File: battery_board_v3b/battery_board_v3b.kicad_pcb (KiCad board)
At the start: 4 copper layers, 88 x 94.5 mm, 204 parts, among them IC2 PCT2075DP,118, IC3 RP2040_QFN56, IC4 LT3652IMSE#PBF, J1 Bypass, J10 Jetson, J11 BM04B-SRSS-TB(LF)(SN), J14 Solar, J15 FC, J16 I2C Multiplexer Breakout, J17 ISS Foot, J18 Screw_Terminal_01x02, J19 BM04B-SRSS-TB(LF)(SN), J2 Heater, J20 CAN1, J21 BM04B-SRSS-TB(LF)(SN), J22 CAN2, J23 Conn_ARM_JTAG_SWD_10, J24 USB_B_Micro, J25 Life Makes Lemonade, J26 BM04B-SRSS-TB(LF)(SN), J27 I2C0 Breakout, J3 BURN, J4 CHARGE, J5 Foot0, J6 Foot1, J7 Foot2, J8 Foot3, J9 RBF, K1 APAN3105, Q1 IRF7458, Q10 IRLML2803, Q11 NDS8434, Q2 IRF7458, Q3 MBT2222ADW1T1, Q4 MMBT2222AT, Q5 MBT2222ADW1T1, Q6 IRLML2803, Q7 IRLML2803, Q8 NDS8434, Q9 NDS8434, SW1 KMR2, SW2 KMR2, U1 R5460N208AA, U10 TLVH431 DBZ SOT-23, U11 MCP25625-E/ML, U12 INA219AxD, U13 MAX706RESA, U14 INA219AxD, U2 1049, U3 TPS54226PWPRPWP14_2P31X2P46-L, U4 1049, U5 TPS54226PWPRPWP14_2P31X2P46-L, U6 TPS7A4501DCQT, U7 ADS1015IDGS, U8 W25Q128JV, U9 AD8495, Y1 Crystal_GND24, Y2 Crystal_GND24

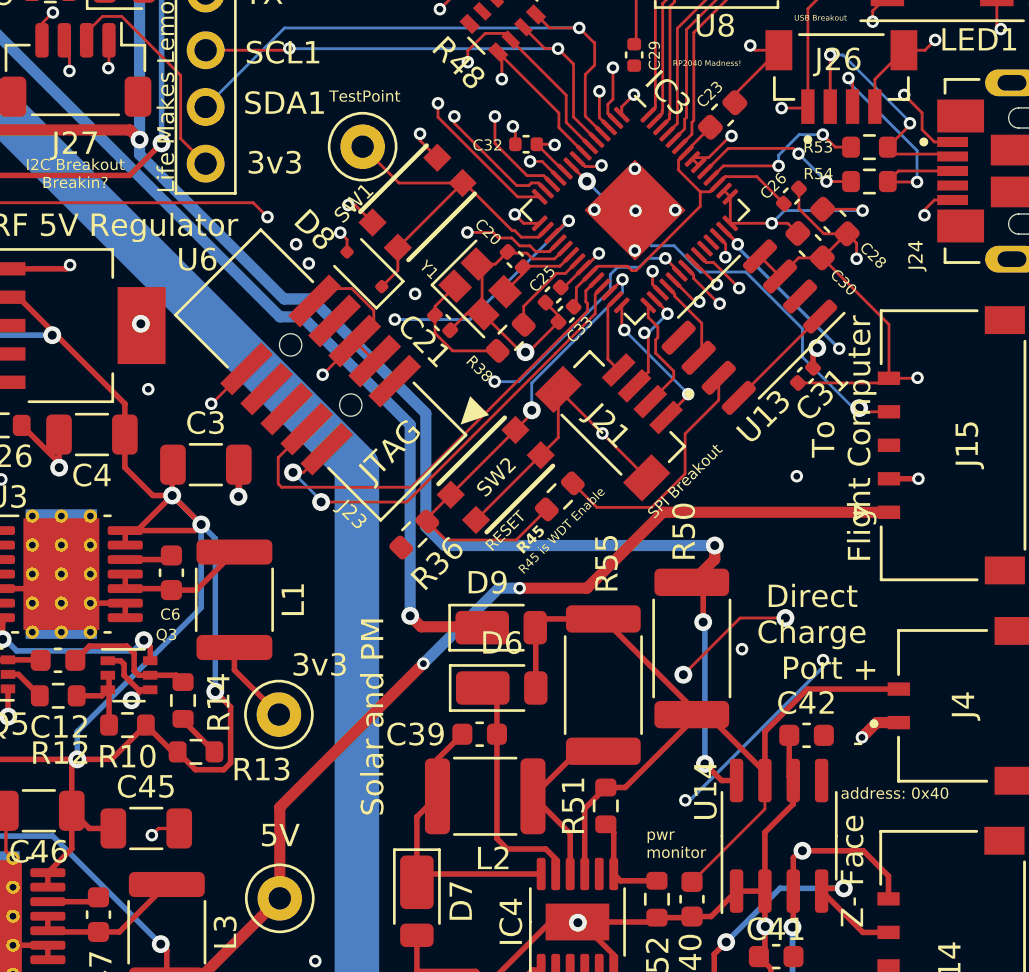
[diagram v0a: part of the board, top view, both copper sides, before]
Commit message: Adjusted Postitioning of Resistors
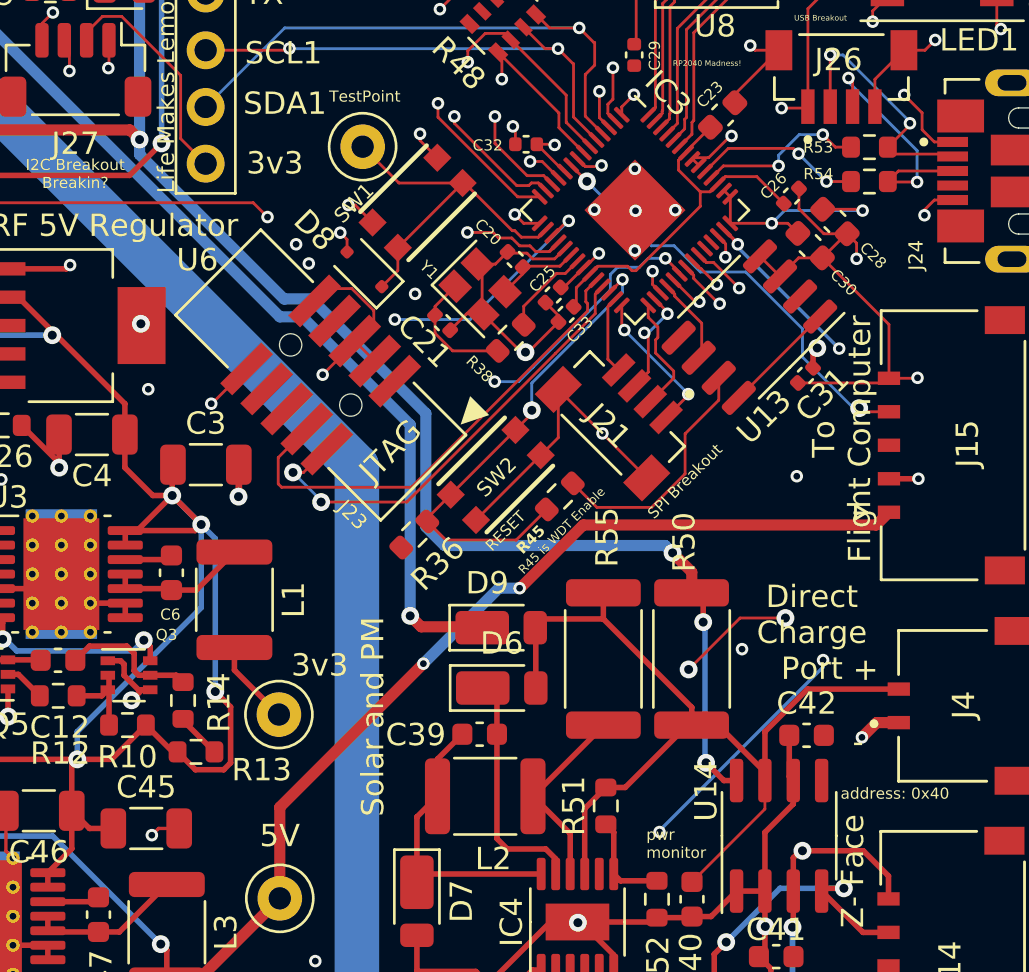
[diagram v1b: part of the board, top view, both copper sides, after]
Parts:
- moved R55 1.17 mm to (176.2, 98.1)
- moved R50 0.47 mm to (180.2, 98.1)
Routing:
- net PACK+: track 215.3 -> 213.1 mm
- net 5V_enable: track 73.6 -> 74.8 mm
- net VBATT_SENSE: track 41.0 -> 42.2 mm
- net Net-(IC4-SENSE): track 8.16 -> 8.66 mm

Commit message: Update battery_board_v3b.kicad_pcb
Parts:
- moved TP9 12.4 mm to (151.2, 115.3)
- moved R1 4.05 mm to (128.0, 110.2)
- moved C46 2.80 mm to (153.7, 105.5)
- moved R61 2.76 mm to (146.2, 113.8)
- moved C47 2.74 mm to (156.4, 109.7)
- moved C43 2.74 mm to (145.3, 105.1)
- moved C45 2.74 mm to (158.5, 105.8)
- moved C48 2.74 mm to (144.2, 111.3)
- moved C49 2.74 mm to (144.2, 109.7)
- moved L3 2.74 mm to (159.4, 110.5)
- moved U5 2.74 mm to (151.2, 109.8)
- moved C44 2.74 mm to (144.2, 106.6)
- moved R18 2.74 mm to (144.2, 108.2)
- moved R16 2.74 mm to (146.5, 107.4)
- moved R20 2.74 mm to (146.5, 110.4)
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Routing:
- net Net-(C5-Pad1): track 8.32 -> 11.3 mm
- net 5V_enable: track 74.8 -> 72.1 mm
- net +5V: track 154.8 -> 156.9 mm
- net Net-(IC2-OS): track 3.65 -> 5.22 mm
- net SDA0: track 165.7 -> 164.5 mm
- net SCL0: track 162.4 -> 161.4 mm
- net B-: track 51.8 -> 51.1 mm
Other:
- board text added: "5V Power Breakout"
- board text added: "5V Regulator"
- board text removed: "Power Breakout"

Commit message: Silkscreen Improvements
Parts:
- moved C4 1.99 mm to (153.8, 90.0)
- moved C3 0.60 mm to (158.5, 90.0)
- moved TP1 0.47 mm to (161.2, 100.6)
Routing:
- net GND: track 322.1 -> 324.3 mm, vias 61 -> 60
- net VBUSP: track 174.4 -> 172.8 mm, vias 6 -> 5
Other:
- board text added: "Battery Heater"
- board text added: "JLCJLCJLCJLC"
- board text removed: "Battery Heater Port"

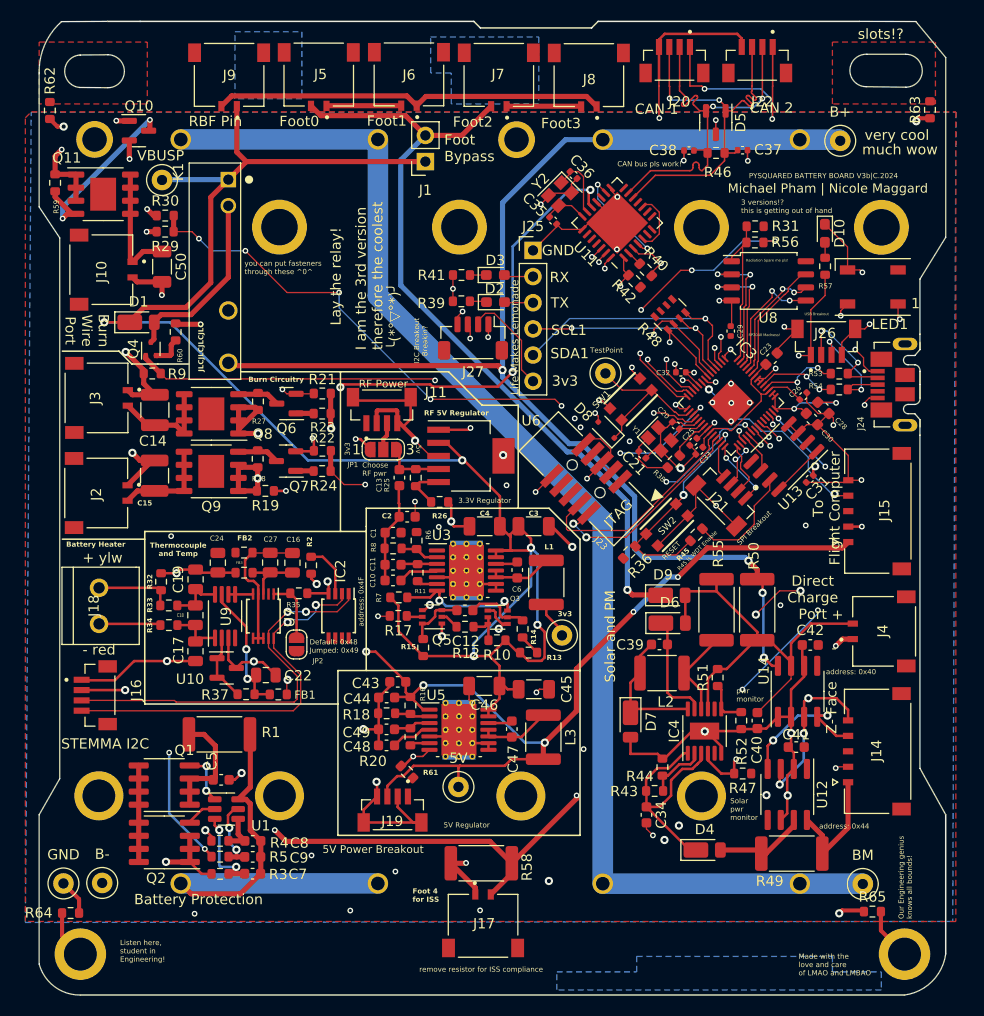
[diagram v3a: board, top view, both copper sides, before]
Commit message: Return of the 12pos Picolock
The return of the king! The 12pos picolock makes a return as a way to interface between the EPS board and the Antenna Top Cap
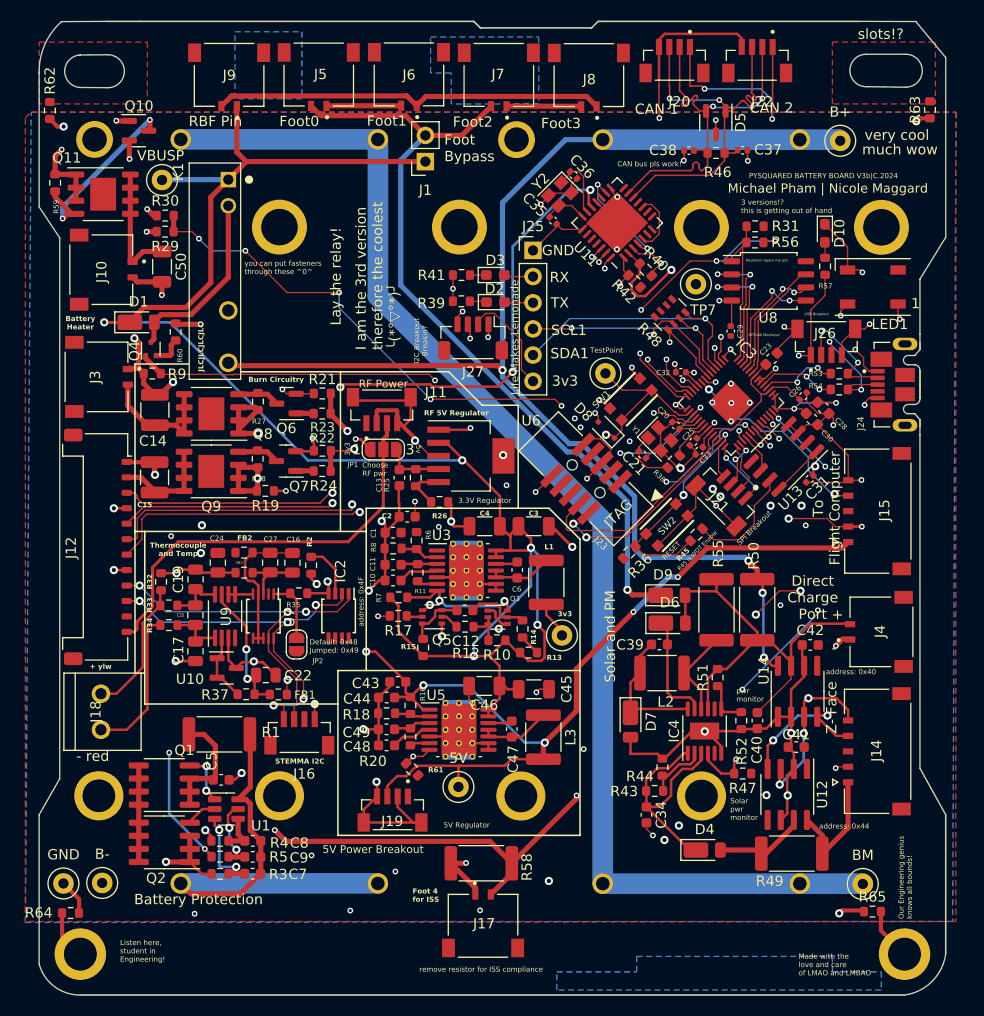
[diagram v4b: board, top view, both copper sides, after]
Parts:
- removed J2: Heater, Battery Board:MOLEX_504050-0291
- added J12: FC_FACE, Connector_Molex:Molex_Pico-Lock_504050-1291_1x12-1MP_P1.50mm_Horizontal, F.Cu at (116.2, 92.0)
- added TP7: RESET, TestPoint:TestPoint_Loop_D1.80mm_Drill1.0mm_Beaded, F.Cu at (174.2, 66.5)
- J3: value BURN -> Heater
- moved J16 19.2 mm to (135.8, 111.2), turned to 180 degrees
- moved J18 10.3 mm to (116.5, 108.0)
- moved J3 2.04 mm to (116.1, 75.5)
- moved R61 0.56 mm to (146.7, 113.6)
- moved J4 0.26 mm to (192.3, 100.2)
- moved C15 0.16 mm to (121.7, 85.2)
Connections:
- net /USBBOOT renamed USBBOOT
- net /V_RF renamed V_RF
- net /~{RESET} renamed ~{RESET}
- C14 pad 1: BURN -> Heater
- C15 pad 1: Heater -> BURN
- J3 pad 2: BURN -> Heater
- Q8 pad 5: BURN -> Heater
- Q8 pad 6: BURN -> Heater
- Q8 pad 7: BURN -> Heater
- Q8 pad 8: BURN -> Heater
- Q9 pad 5: Heater -> BURN
- Q9 pad 6: Heater -> BURN
- Q9 pad 7: Heater -> BURN
- Q9 pad 8: Heater -> BURN
- R21 pad 1: ENAB_BURN -> ENAB_HEATER
- R22 pad 1: ENAB_HEATER -> ENAB_BURN
- R23 pad 2: ENAB_BURN -> ENAB_HEATER
- R24 pad 2: ENAB_HEATER -> ENAB_BURN
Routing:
- net USB_D+: track 7.58 -> 87.3 mm, vias 2 -> 4
- net USB_D-: track 7.57 -> 87.0 mm, vias 2 -> 4
- net USBBOOT: track 16.2 -> 68.1 mm, vias 0 -> 2
- net ~{RESET}: track 38.8 -> 80.2 mm, vias 3 -> 4
- net V_RF: track 3.67 -> 41.8 mm
- net Net-(U11-RESET): track 1.53 -> 12.5 mm, vias 0 -> 1
- net Net-(J18-Pin_1): track 6.00 -> 15.1 mm
- net Net-(J18-Pin_2): track 7.62 -> 13.9 mm
- net ENAB_HEATER: track 46.6 -> 50.9 mm
- net +3V3: track 72.5 -> 68.3 mm, vias 26 -> 29
- net D0: track 18.2 -> 21.4 mm, vias 2 -> 3
- net GND: track 324.3 -> 321.2 mm, vias 60 -> 66
- net Heater: track 9.71 -> 12.4 mm
- net SDA0: track 164.3 -> 162.9 mm, vias 6 -> 7
- net SCL0: track 161.4 -> 162.3 mm, vias 7 -> 10
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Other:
- board text removed: "Burn Wire Port"
